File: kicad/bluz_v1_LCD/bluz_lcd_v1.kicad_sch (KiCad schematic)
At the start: 100 parts, among them J10 Conn, J11 Conn, J12 BTAnt, J2 Conn, J3 Conn, J4 Conn, J40 LS013B7DH05, J5 Conn, J6 Conn, J7 Conn, J8 Conn, J9 USB_C_Receptacle_PowerOnly_6P, M1 Z3OC1T8219731, Q1 NTA4153NT1G, Q2 RUM002N05, Q3 NTA4153NT1G, Q4 NTA4151PT1G, Q5 NTA4153NT1G, Q6 NTA4153NT1G, U1 MCP73831, U2 REF35180QDBVR, U3 TLV3201AIDCK, U4 AP3015KTR, U6 PAM8904EGPR, U7 TPS627451DSSR, Y1 NX1612SA-32MHz, Y2 NX2012SA-32.768

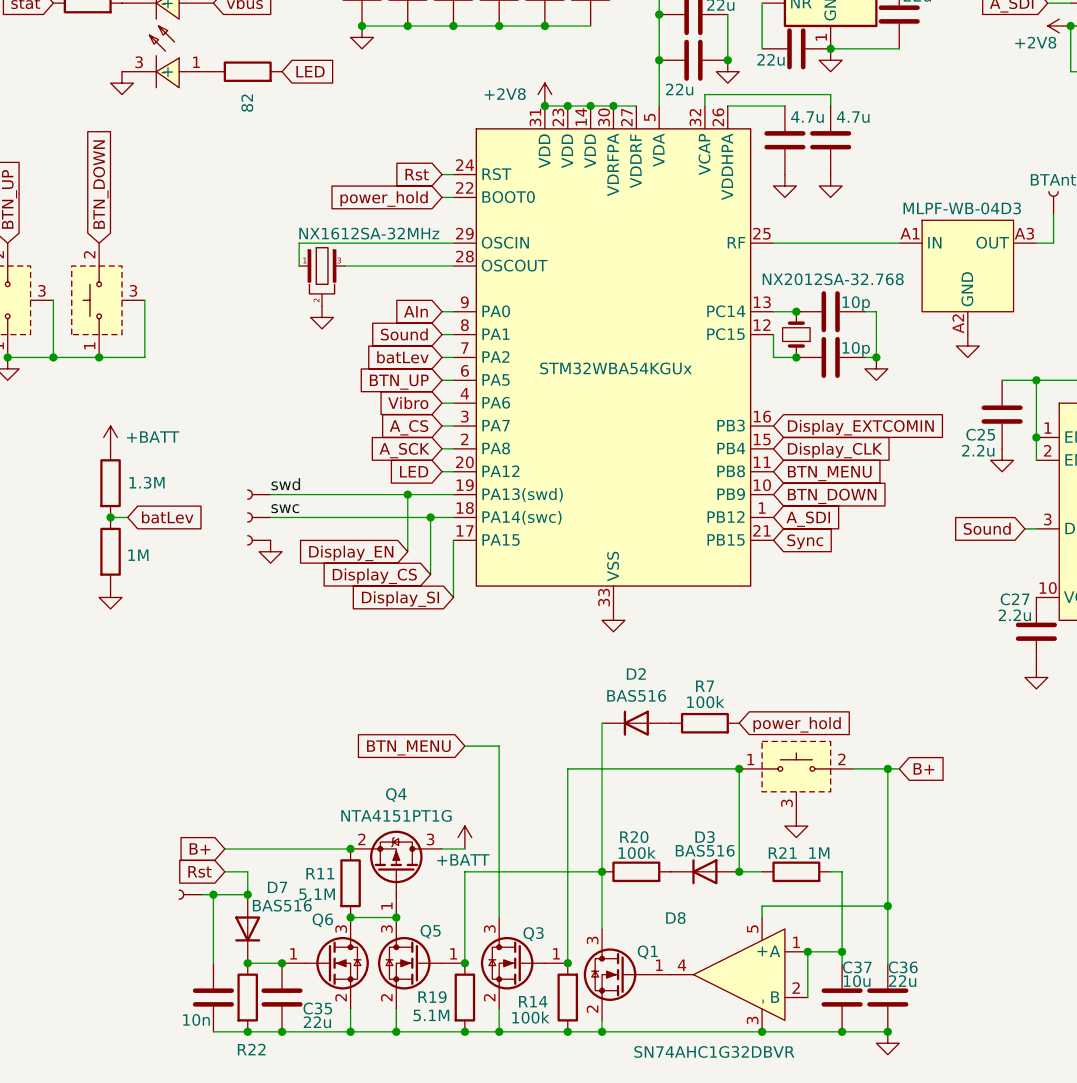
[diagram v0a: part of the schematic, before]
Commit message: переименовано: kicad/bluz_v1_LED/2024-05-07_07-39-39.kicad_sym -> kicad/bluz_v1_LCD/2024-05-07_07-39-39.kicad_sym 	переименовано: kicad/bluz_v1_LED/CSPG6_1P05X1P65_STM-L.kicad_mod -> kicad/bluz_v1_LCD/CSPG6_1P05X1P65_STM-L.kicad_mod 	переименовано: kicad/bluz_v1_LED/CSPG6_1P05X1P65_STM-M.kicad_mod -> kicad/bluz_v1_LCD/CSPG6_1P05X1P65_STM-M.kicad_mod 	переименовано: kicad/bluz_v1_LED/CSPG6_1P05X1P65_STM.kicad_mod -> kicad/bluz_v1_LCD/CSPG6_1P05X1P65_STM.kicad_mod 	новый файл:    kicad/bluz_v1_LCD/bluz_lcd_v1-backups/bluz_lcd_v1-2026-10-17_154510.zip 	новый файл:    kicad/bluz_v1_LCD/bluz_lcd_v1-backups/bluz_lcd_v1-2026-10-17_155607.zip 	переименовано: kicad/bluz_v1_LED/bluz_v1.kicad_pcb -> kicad/bluz_v1_LCD/bluz_lcd_v1.kicad_pcb 	переименовано: kicad/bluz_v1_LED/bluz_v1.kicad_prl -> kicad/bluz_v1_LCD/bluz_lcd_v1.kicad_prl 	переименовано: kicad/bluz_v1_LED/bluz_v1.kicad_pro -> kicad/bluz_v1_LCD/bluz_lcd_v1.kicad_pro 	переименовано: kicad/bluz_v1_LED/bluz_v1.kicad_sch -> kicad/bluz_v1_LCD/bluz_lcd_v1.kicad_sch 	переименовано: kicad/bluz_v1_LED/fp-info-cache -> kicad/bluz_v1_LCD/fp-info-cache 	новый файл:    kicad/bluz_v1_LCD/gerber/mill_config.txt 	новый файл:    kicad/bluz_v1_LCD/gerber/mk-gcode.sh 	переименовано: kicad/bluz_v1_LED/gerber/mk-gerber.sh -> kicad/bluz_v1_LCD/gerber/mk-gerber.sh 	удалено:       kicad/bluz_v1_LED/bluz_v1-backups/bluz_v1-2026-09-14_181225.zip 	удалено:       kicad/bluz_v1_LED/bluz_v1-backups/bluz_v1-2026-09-15_141616.zip 	удалено:       kicad/bluz_v1_LED/bluz_v1-backups/bluz_v1-2026-09-15_144107.zip 	удалено:       kicad/bluz_v1_LED/bluz_v1-backups/bluz_v1-2026-09-15_145150.zip 	удалено:       kicad/bluz_v1_LED/bluz_v1-backups/bluz_v1-2026-09-15_150420.zip 	удалено:       kicad/bluz_v1_LED/bluz_v1-backups/bluz_v1-2026-09-15_155235.zip 	удалено:       kicad/bluz_v1_LED/bluz_v1-backups/bluz_v1-2026-09-17_183048.zip 	удалено:       kicad/bluz_v1_LED/bluz_v1-backups/bluz_v1-2026-09-17_183700.zip 	удалено:       kicad/bluz_v1_LED/bluz_v1-backups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
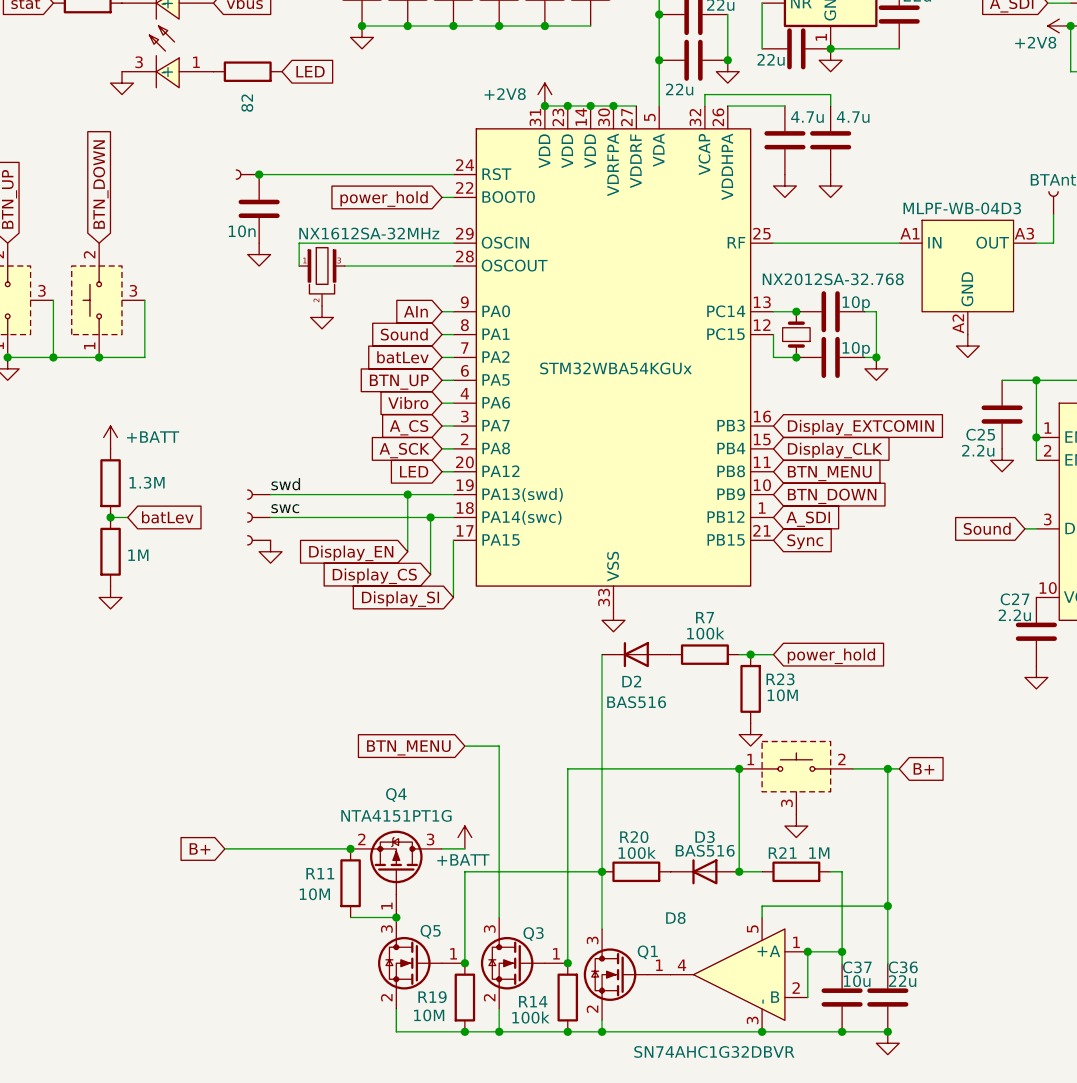
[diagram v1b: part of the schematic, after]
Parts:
- removed C35: 22u, Capacitor_SMD:C_0402_1005Metric, symbol Device:C
- removed D7: BAS516, Diode_SMD:D_SOD-523, symbol Diode:BAS516
- removed Q6: NTA4153NT1G, Package_TO_SOT_SMD:SOT-723, symbol Transistor_FET:IRLML2060
- removed R22: 5.1M, Resistor_SMD:R_0402_1005Metric, symbol Device:R
- added R23: 10M, Resistor_SMD:R_0402_1005Metric, symbol Device:R
- R11, R19: value 5.1M -> 10M
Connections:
- net GND: now also R23.1
- net power_hold: now also R23.2
- net Rst: no longer names the net of C18.2, D1.24 (RST), J2.1
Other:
- moved on the sheet: D2, R7
